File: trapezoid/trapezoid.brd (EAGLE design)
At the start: 75.2 x 28.6 mm, 32 parts, among them IC2 LGD20H, U1 MMA8452Q, U2 microSD, U4 MCP73831, Y1 CRYSTAL.ABS25

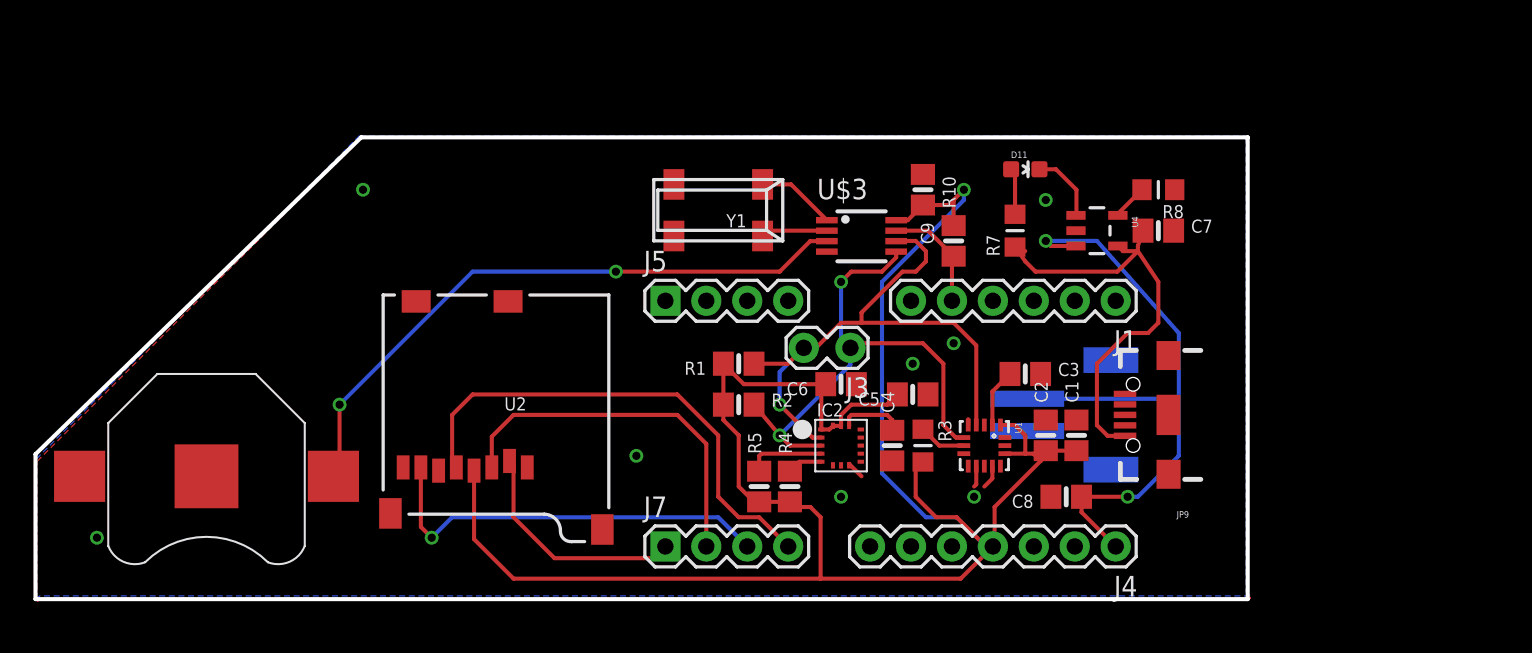
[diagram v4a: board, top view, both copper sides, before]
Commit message: moved usb out form under pro mini
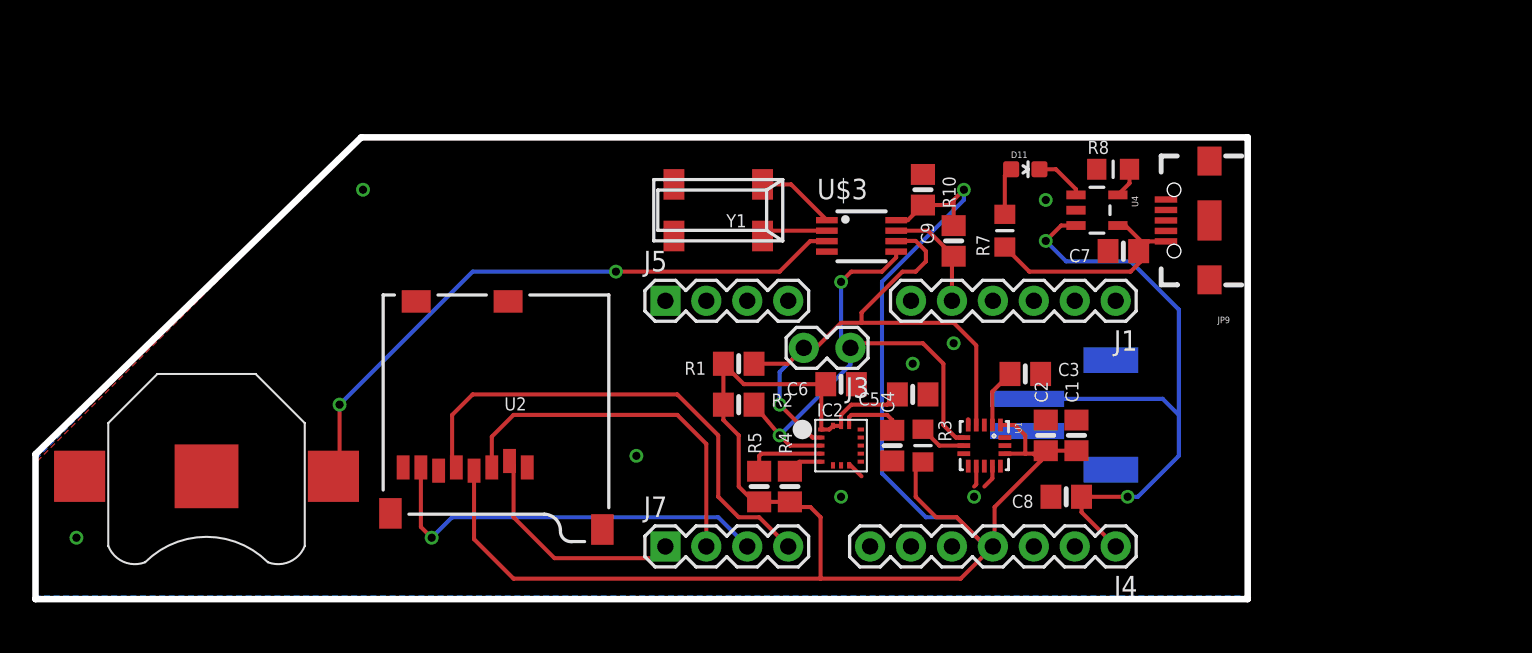
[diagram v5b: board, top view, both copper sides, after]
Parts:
- moved JP9 12.3 mm to (72.8, 23.5)
- moved R8 3.08 mm to (66.9, 26.7), turned to 0 degrees
- moved C7 2.51 mm to (67.5, 21.6), turned to 180 degrees
- moved U4 1.27 mm to (65.9, 24.1)
- moved R7 0.63 mm to (60.1, 22.9)
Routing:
- net VIN: track 27.8 -> 14.1 mm
- net STAT: track 4.43 -> 3.13 mm
- net V_RAW: track 41.3 -> 42.2 mm
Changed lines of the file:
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@@
 <setting verticaltext="up"/>
 </settings>
-<grid distance="0.05" unitdist="inch" unit="inch" style="lines" multiple="1" display="yes" altdistance="0.025" altunitdist="inch" altunit="inch"/>
+<grid distance="0.025" unitdist="inch" unit="inch" style="lines" multiple="1" display="yes" altdistance="0.005" altunitdist="inch" altunit="inch"/>
 <layers>
 <layer number="1" name="Top" color="4" fill="1" visible="yes" active="yes"/>
@@
 <layer number="45" name="Holes" color="7" fill="1" visible="yes" active="yes"/>
 <layer number="46" name="Milling" color="3" fill="1" visible="no" active="yes"/>
-<layer number="47" name="Measures" color="7" fill="1" visible="yes" active="yes"/>
+<layer number="47" name="Measures" color="7" fill="1" visible="no" active="yes"/>
 <layer number="48" name="Document" color="7" fill="1" visible="no" active="yes"/>
 <layer number="49" name="Reference" color="7" fill="1" visible="no" active="yes"/>
@@
 <board>
 <plain>
-<wire x1="0" y1="0" x2="75.21" y2="0" width="0.254" layer="20"/>
-<wire x1="75.21" y1="0" x2="75.21" y2="28.65" width="0.254" layer="20"/>
-<wire x1="20.21" y1="28.65" x2="75.21" y2="28.65" width="0.254" layer="20"/>
-<wire x1="20.21" y1="28.65" x2="0" y2="8.99" width="0.254" layer="20"/>
-<wire x1="0" y1="8.99" x2="0" y2="0" width="0.254" layer="20"/>
+<wire x1="0" y1="0" x2="75.21" y2="0" width="0.4064" layer="20"/>
+<wire x1="75.21" y1="0" x2="75.21" y2="28.65" width="0.4064" layer="20"/>
+<wire x1="20.21" y1="28.65" x2="75.21" y2="28.65" width="0.4064" layer="20"/>
+<wire x1="20.21" y1="28.65" x2="0" y2="8.99" width="0.4064" layer="20"/>
+<wire x1="0" y1="8.99" x2="0" y2="0" width="0.4064" layer="20"/>
 </plain>
 <attributes>
@@
 <element name="C5" library="microbuilder" package="0805-NO" value="10uF" x="54.425" y="12.7" rot="R180"/>
 <element name="C6" library="microbuilder" package="0805-NO" value="0.1uF" x="49.98" y="13.335" rot="R180"/>
-<element name="C7" library="microbuilder" package="0805-NO" value="4.7uF" x="69.665" y="22.86"/>
+<element name="C7" library="microbuilder" package="0805-NO" value="4.7uF" x="67.495" y="21.59" rot="R180"/>
 <element name="C8" library="microbuilder" package="0805-NO" value="4.7uF" x="63.95" y="6.35" rot="R180"/>
 <element name="D11" library="SparkFun-LED" package="LED-0603" value="RED" x="61.41" y="26.67" rot="R270">
@@
 <attribute name="PROD_ID" value="CONN-08352" x="65.22" y="11.43" size="1.778" layer="28" rot="MR90" display="off"/>
 </element>
-<element name="JP9" library="SparkFun-Connectors" package="USB-AB-MICRO-SMD_V03" value="Micro USB" x="70.3" y="11.43" rot="R180">
-<attribute name="PROD_ID" value="CONN-11794" x="70.3" y="11.43" size="1.778" layer="27" rot="R180" display="off"/>
+<element name="JP9" library="SparkFun-Connectors" package="USB-AB-MICRO-SMD_V03" value="Micro USB" x="72.84" y="23.495" rot="R180">
+<attribute name="PROD_ID" value="CONN-11794" x="72.84" y="23.495" size="1.778" layer="27" rot="R180" display="off"/>
 </element>
 <element name="R1" library="microbuilder" package="0805-NO" value="10K" x="43.63" y="14.605" rot="R180"/>
@@
 <element name="R4" library="microbuilder" package="0805-NO" value="10K" x="46.805" y="6.985" rot="R90"/>
 <element name="R5" library="microbuilder" package="0805-NO" value="10K" x="44.9" y="6.985" rot="R90"/>
-<element name="R7" library="microbuilder" package="_0805MP" value="330" x="60.775" y="22.86" rot="R90"/>
-<element name="R8" library="microbuilder" package="_0805MP" value="2.0k" x="69.665" y="25.4" rot="R180"/>
+<element name="R7" library="microbuilder" package="_0805MP" value="330" x="60.14" y="22.86" rot="R90"/>
+<element name="R8" library="microbuilder" package="_0805MP" value="2.0k" x="66.86" y="26.67"/>
 <element name="U1" library="SparkFun" package="QFN-16_0.5MM" value="MMA8452Q" x="58.87" y="9.525" rot="R270"/>
 <element name="U2" library="SparkFun" package="MICRO-SD-SOCKET-PP" value="microSD" x="21.57" y="18.87" rot="R180"/>
-<element name="U4" library="SparkFun-PowerIC" package="SOT23-5" value="MCP73831" x="65.855" y="22.86" rot="R270">
-<attribute name="PROD_ID" value="IC-09995" x="65.855" y="22.86" size="1.778" layer="27" rot="R270" display="off"/>
+<element name="U4" library="SparkFun-PowerIC" package="SOT23-5" value="MCP73831" x="65.855" y="24.13" rot="R270">
+<attribute name="PROD_ID" value="IC-09995" x="65.855" y="24.13" size="1.778" layer="27" rot="R270" display="off"/>
 </element>
 <element name="U$3" library="sharkdunio" package="8U-SOP" value="DS1339BDS1339B" x="51.25" y="22.86"/>
@@
 <vertex x="0.15" y="-0.15"/>
 </polygon>
-<via x="3.81" y="3.81" extent="1-16" drill="0.508"/>
+<via x="2.54" y="3.81" extent="1-16" drill="0.508"/>
 <via x="20.32" y="25.4" extent="1-16" drill="0.508"/>
 </signal>
@@
 <wire x1="64.9" y1="6.35" x2="64.9" y2="5.39" width="0.254" layer="1"/>
 <wire x1="64.9" y1="5.39" x2="67.02" y2="3.27" width="0.254" layer="1"/>
-<wire x1="64.5549" y1="21.91" x2="62.995" y2="21.91" width="0.254" layer="1"/>
-<wire x1="62.995" y1="21.91" x2="62.68" y2="22.225" width="0.254" layer="1"/>
 <via x="62.68" y="22.225" extent="1-16" drill="0.508"/>
-<wire x1="62.68" y1="22.225" x2="65.855" y2="22.225" width="0.254" layer="16"/>
-<wire x1="65.855" y1="22.225" x2="70.935" y2="16.51" width="0.254" layer="16"/>
-<wire x1="70.935" y1="16.51" x2="70.935" y2="11.43" width="0.254" layer="16"/>
+<wire x1="70.935" y1="17.965" x2="70.935" y2="11.43" width="0.254" layer="16"/>
 <wire x1="70.935" y1="11.43" x2="70.935" y2="8.89" width="0.254" layer="16"/>
 <via x="67.76" y="6.35" extent="1-16" drill="0.508"/>
@@
 <wire x1="68.395" y1="6.35" x2="70.935" y2="8.89" width="0.254" layer="16"/>
 <contactref element="J4" pad="1"/>
+<wire x1="64.5549" y1="23.18" x2="63.635" y2="23.18" width="0.254" layer="1"/>
+<wire x1="63.635" y1="23.18" x2="62.68" y2="22.225" width="0.254" layer="1"/>
+<wire x1="70.935" y1="17.965" x2="67.945" y2="20.955" width="0.254" layer="16"/>
+<wire x1="67.945" y1="20.955" x2="63.95" y2="20.955" width="0.254" layer="16"/>
+<wire x1="63.95" y1="20.955" x2="62.68" y2="22.225" width="0.254" layer="16"/>
 </signal>
 <signal name="N$3">
@@
 <contactref element="D11" pad="A"/>
 <contactref element="R7" pad="2"/>
-<wire x1="60.775" y1="23.876" x2="60.775" y2="26.428" width="0.254" layer="1"/>
 <wire x1="60.775" y1="26.428" x2="60.533" y2="26.67" width="0.254" layer="1"/>
+<wire x1="60.14" y1="23.876" x2="60.14" y2="26.277" width="0.254" layer="1"/>
+<wire x1="60.14" y1="26.277" x2="60.533" y2="26.67" width="0.254" layer="1"/>
 </signal>
 <signal name="PROG">
 <contactref element="U4" pad="5"/>
 <contactref element="R8" pad="2"/>
-<wire x1="67.1551" y1="23.81" x2="67.1551" y2="23.9061" width="0.254" layer="1"/>
-<wire x1="67.1551" y1="23.9061" x2="68.649" y2="25.4" width="0.254" layer="1"/>
+<wire x1="67.876" y1="26.67" x2="67.876" y2="25.8009" width="0.254" layer="1"/>
+<wire x1="67.876" y1="25.8009" x2="67.1551" y2="25.08" width="0.254" layer="1"/>
 </signal>
 <signal name="STAT">
@@
 <contactref element="U4" pad="1"/>
 <wire x1="62.287" y1="26.67" x2="63.315" y2="26.67" width="0.254" layer="1"/>
-<wire x1="63.315" y1="26.67" x2="64.585" y2="25.4" width="0.254" layer="1"/>
-<wire x1="64.585" y1="25.4" x2="64.585" y2="23.8401" width="0.254" layer="1"/>
-<wire x1="64.585" y1="23.8401" x2="64.5549" y2="23.81" width="0.254" layer="1"/>
+<wire x1="64.5549" y1="25.08" x2="64.5549" y2="25.4301" width="0.254" layer="1"/>
+<wire x1="64.5549" y1="25.4301" x2="63.315" y2="26.67" width="0.254" layer="1"/>
 </signal>
 <signal name="VIN">
@@
 <contactref element="R7" pad="1"/>
 <contactref element="C7" pad="1"/>
-<wire x1="67.6" y1="10.13" x2="66.52" y2="10.13" width="0.254" layer="1"/>
-<wire x1="66.52" y1="10.13" x2="65.855" y2="10.795" width="0.254" layer="1"/>
-<wire x1="65.855" y1="10.795" x2="65.855" y2="14.605" width="0.254" layer="1"/>
-<wire x1="65.855" y1="14.605" x2="67.76" y2="16.51" width="0.254" layer="1"/>
-<wire x1="67.76" y1="16.51" x2="69.03" y2="16.51" width="0.254" layer="1"/>
-<wire x1="69.03" y1="16.51" x2="69.665" y2="17.145" width="0.254" layer="1"/>
-<wire x1="69.665" y1="17.145" x2="69.665" y2="19.685" width="0.254" layer="1"/>
-<wire x1="69.665" y1="19.685" x2="68.395" y2="21.59" width="0.254" layer="1"/>
-<wire x1="68.395" y1="21.59" x2="67.4751" y2="21.59" width="0.254" layer="1"/>
-<wire x1="67.4751" y1="21.59" x2="67.1551" y2="21.91" width="0.254" layer="1"/>
-<wire x1="68.395" y1="21.59" x2="68.395" y2="21.905" width="0.254" layer="1"/>
-<wire x1="68.395" y1="21.905" x2="68.715" y2="22.86" width="0.254" layer="1"/>
-<wire x1="60.775" y1="21.844" x2="61.41" y2="21.59" width="0.254" layer="1"/>
-<wire x1="60.775" y1="21.844" x2="61.41" y2="20.955" width="0.254" layer="1"/>
-<wire x1="61.41" y1="20.955" x2="62.045" y2="20.32" width="0.254" layer="1"/>
-<wire x1="62.045" y1="20.32" x2="67.125" y2="20.32" width="0.254" layer="1"/>
-<wire x1="67.125" y1="20.32" x2="68.395" y2="21.59" width="0.254" layer="1"/>
+<wire x1="70.14" y1="22.195" x2="69.05" y2="22.195" width="0.254" layer="1"/>
+<wire x1="69.05" y1="22.195" x2="68.83" y2="21.975" width="0.254" layer="1"/>
+<wire x1="68.83" y1="21.975" x2="68.445" y2="21.59" width="0.254" layer="1"/>
+<wire x1="67.1551" y1="23.18" x2="67.625" y2="23.18" width="0.254" layer="1"/>
+<wire x1="67.625" y1="23.18" x2="68.83" y2="21.975" width="0.254" layer="1"/>
+<wire x1="67.945" y1="20.32" x2="68.58" y2="20.955" width="0.254" layer="1"/>
+<wire x1="68.58" y1="20.955" x2="68.58" y2="21.455" width="0.254" layer="1"/>
+<wire x1="68.58" y1="21.455" x2="68.445" y2="21.59" width="0.254" layer="1"/>
+<wire x1="67.945" y1="20.32" x2="61.664" y2="20.32" width="0.254" layer="1"/>
+<wire x1="61.664" y1="20.32" x2="60.14" y2="21.844" width="0.254" layer="1"/>
 </signal>
 <signal name="N$2">

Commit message: put onto 0.025in grid
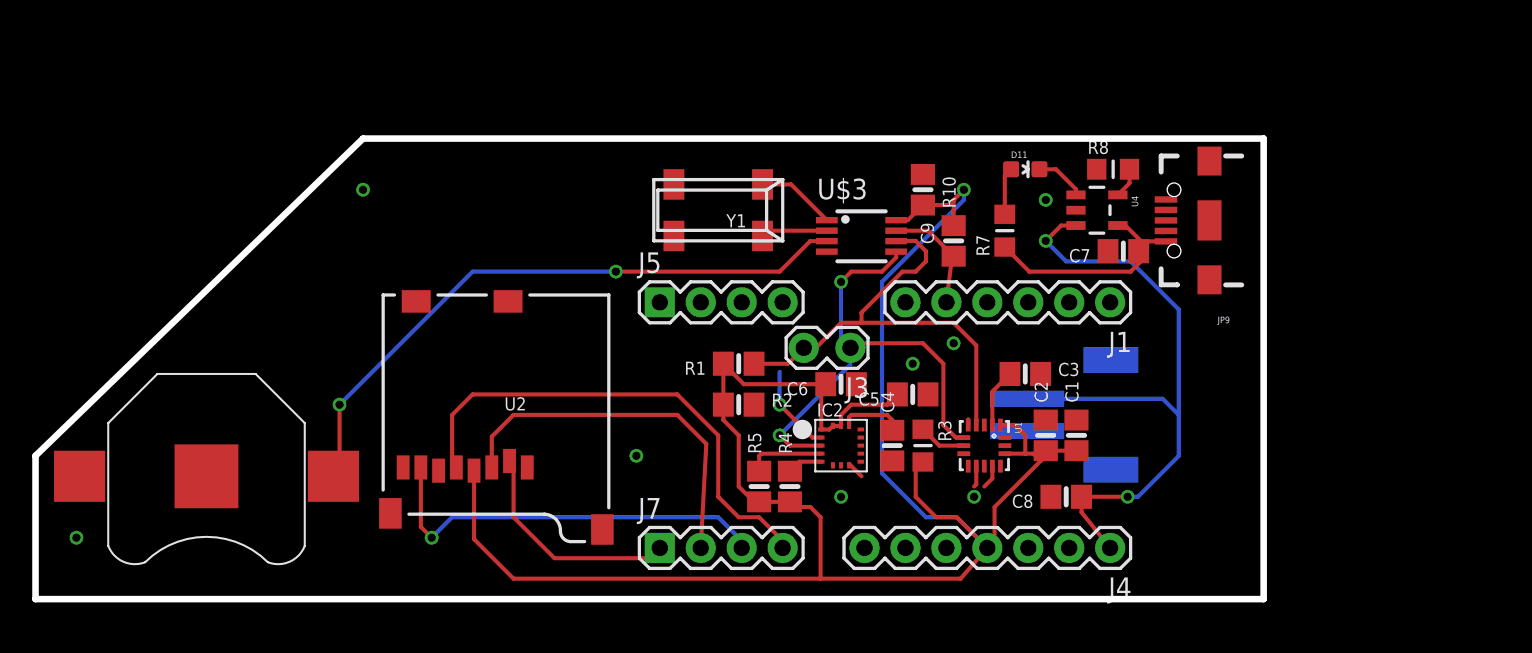
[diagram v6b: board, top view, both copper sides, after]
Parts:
- moved J1 0.36 mm to (66.7, 18.4)
- moved J5 0.36 mm to (38.7, 18.4)
- moved J4 0.36 mm to (66.7, 3.17)
- moved J7 0.36 mm to (38.7, 3.17)
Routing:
- net SDA: track 33.1 -> 28.4 mm
- net SCL: track 37.0 -> 34.1 mm
- net +3V3: track 130.5 -> 130.0 mm
- removed copper zone on layer 1, net GND
- removed copper zone on layer 16, net GND
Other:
- board size 75.2 x 28.6 mm -> 76.2 x 28.6 mm

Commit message: corectly possitoned i2c pins
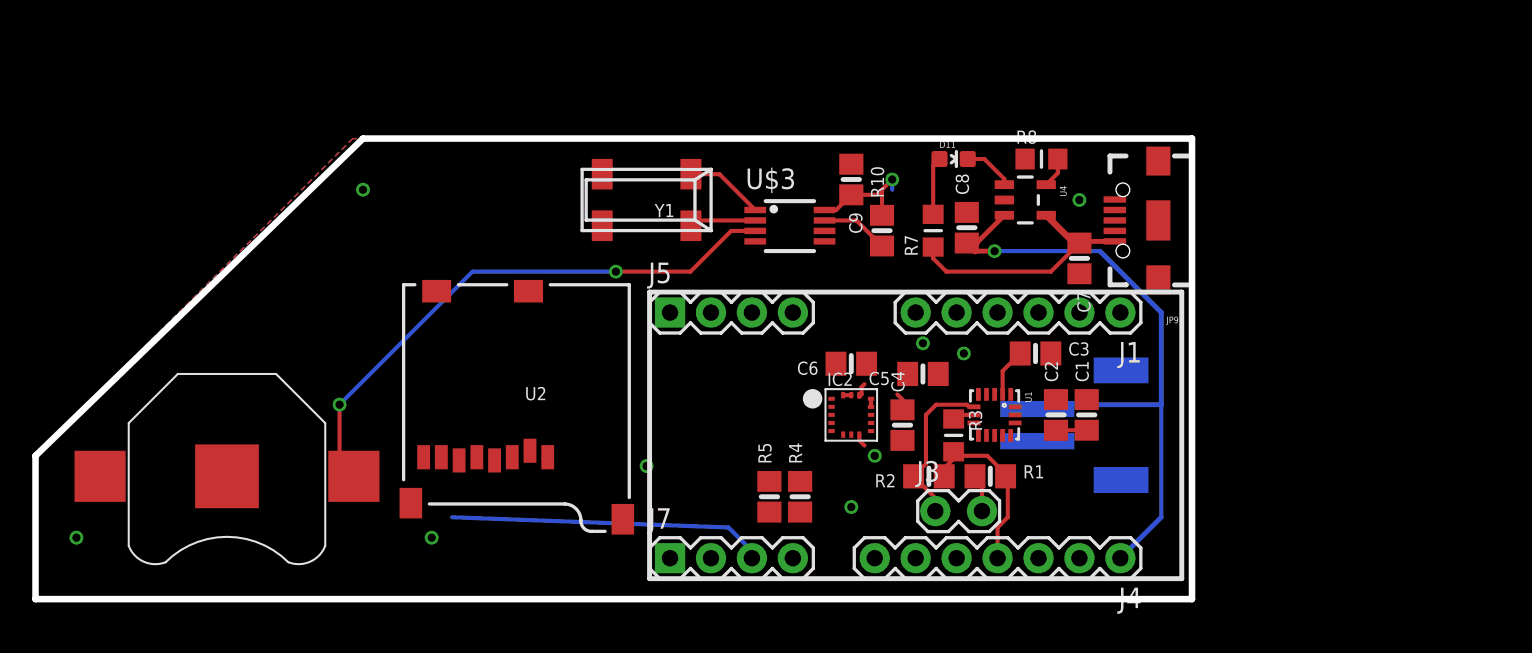
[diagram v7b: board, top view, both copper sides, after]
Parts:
- moved C8 17.8 mm to (57.8, 23.0), turned to 90 degrees
- moved R1 17.1 mm to (59.2, 7.62), turned to 0 degrees
- moved R2 12.6 mm to (55.4, 7.62), turned to 180 degrees
- moved J3 11.6 mm to (56.0, 5.46), turned to 0 degrees
- moved U4 4.49 mm to (61.4, 24.8)
- moved C9 4.49 mm to (50.6, 26.0)
- moved U$3 4.49 mm to (46.8, 23.5)
- moved Y1 4.49 mm to (37.9, 24.8)
- moved R10 4.49 mm to (52.5, 22.9)
- moved R8 4.49 mm to (62.4, 27.3)
- moved D11 4.49 mm to (57.0, 27.3)
- moved R7 4.45 mm to (55.7, 22.9)
- moved JP9 3.17 mm to (69.7, 23.5)
- moved C7 2.76 mm to (64.8, 21.1), turned to 270 degrees
- moved IC2 2.01 mm to (50.6, 11.4)
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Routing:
- net +3V3: track 130.0 -> 21.5 mm
- net SCL: track 34.1 -> 2.34 mm, vias 1 -> 0
- net SCK: track 31.2 -> 0.00 mm
- net MOSI: track 23.0 -> 0.00 mm
- net SDA: track 28.4 -> 10.1 mm, vias 2 -> 0
- net SD_CS: track 14.4 -> 0.00 mm
- net MISO: track 25.8 -> 20.1 mm
- net SDO/SAO: track 5.31 -> 0.00 mm
- net N$4: track 39.0 -> 35.3 mm
- net SQW/INT: track 7.15 -> 4.37 mm
- net GND: track 4.33 -> 1.59 mm
- net VIN: track 14.1 -> 16.4 mm
- net CS_3.3V: track 2.19 -> 0.00 mm
- net SA0: track 3.49 -> 1.37 mm
- net N$3: track 4.04 -> 2.08 mm
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- added copper zone on layer 1, net GND
- added copper zone on layer 16, net GND
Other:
- board size 76.2 x 28.6 mm -> 71.8 x 28.6 mm
